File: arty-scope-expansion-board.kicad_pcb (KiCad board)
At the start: 4 copper layers, 109 x 86 mm, 131 parts, among them J1 PMOD_A, J2 PMOD_B, J3 PMOD_C, J4 PMOD_D, J5 Conn_Coaxial, J6 Conn_01x02_Pin, J7 Conn_Coaxial, U1 AD9288, U10 MCP1826S, U11 MIC5504-3.3YM5, U12 AD8132ARZ, U13 AD8370AREZ-RL7, U14 AD8132ARZ, U2 74LS374, U3 74LS374, U4 AD8370AREZ-RL7, U5 AD8132ARZ, U6 AD8132ARZ, U7 MCP4822, U8 74AHCT541, U9 74AHCT541

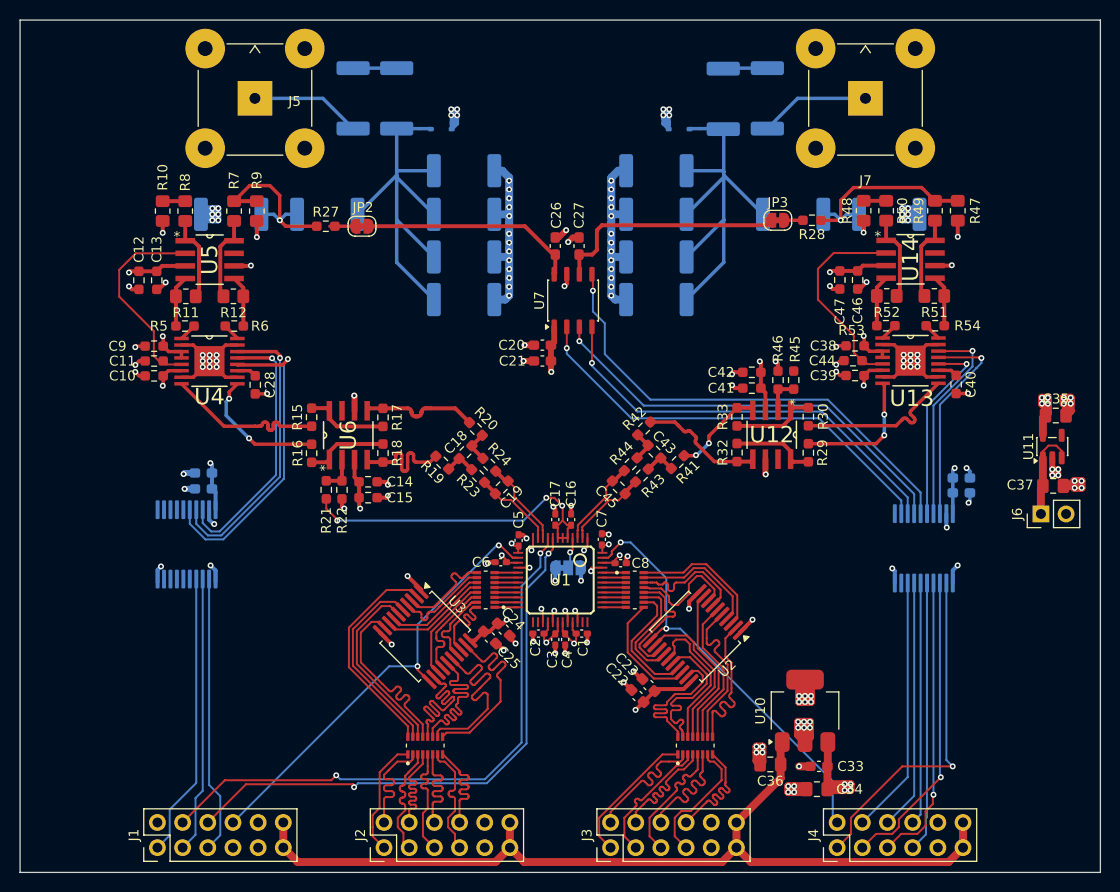
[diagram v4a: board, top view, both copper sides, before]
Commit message: [feat] Changed input stage routing, corrected DRC errors, added some silk labels
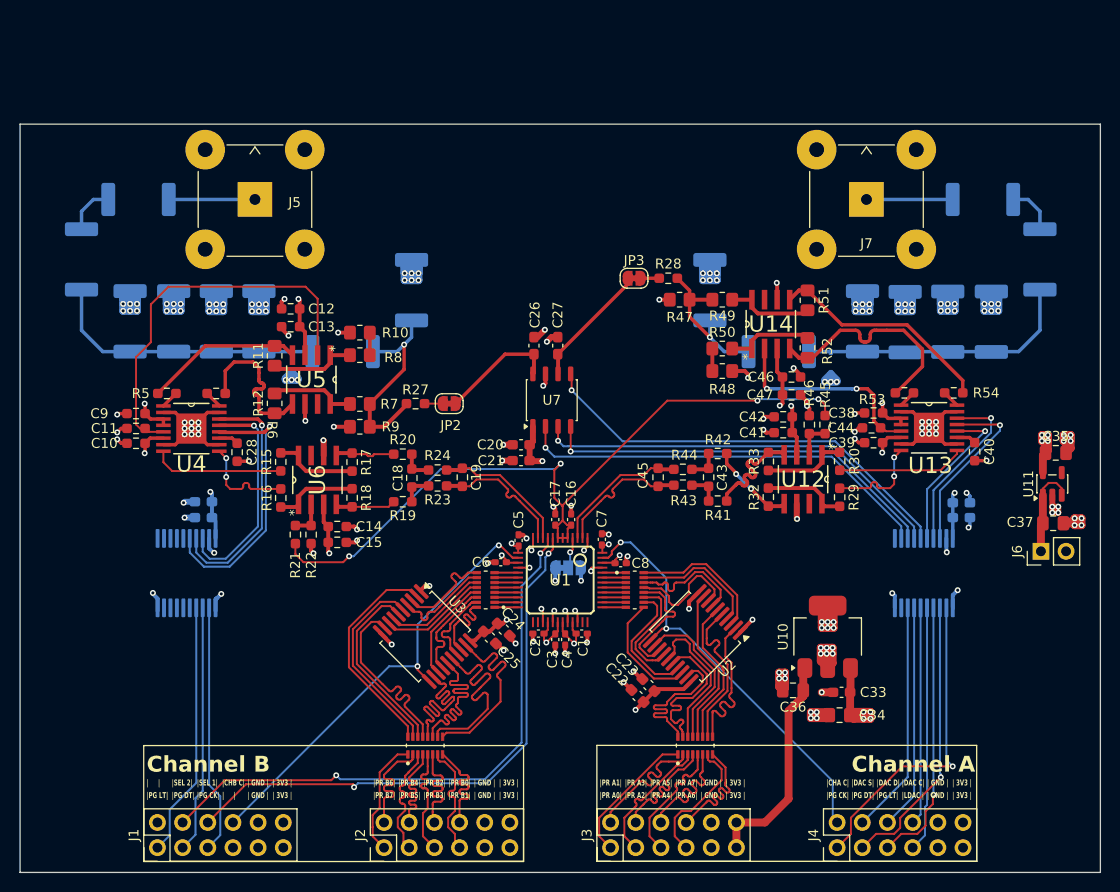
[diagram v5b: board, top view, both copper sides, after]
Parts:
- moved R35 37.1 mm to (213.5, 67.4), turned to 90 degrees
- moved R2 37.0 mm to (126.6, 67.4), turned to 90 degrees
- moved R34 35.8 mm to (218.4, 61.1)
- moved R13 35.7 mm to (121.7, 61.1)
- moved R36 31.3 mm to (209.1, 67.4), turned to 90 degrees
- moved R26 31.2 mm to (131.0, 67.4), turned to 90 degrees
- moved R47 29.5 mm to (182.1, 65.2), turned to 0 degrees
- moved D4 28.1 mm to (197.3, 71.5), turned to -90 degrees
- moved D3 27.9 mm to (142.9, 71.5), turned to -90 degrees
- moved R25 25.8 mm to (135.3, 67.4), turned to 90 degrees
- moved R38 25.2 mm to (204.8, 67.5), turned to 90 degrees
- moved R9 24.1 mm to (149.8, 78.0), turned to 0 degrees
- moved R31 24.0 mm to (212.7, 55.1), turned to 180 degrees
- moved R1 23.9 mm to (127.5, 55.1), turned to 0 degrees
- moved R10 23.4 mm to (149.8, 68.5), turned to 0 degrees
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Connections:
- J1 pad 11: VIN_3.3V -> unconnected-(J1-Pin_11-Pad11)
- J1 pad 12: VIN_3.3V -> unconnected-(J1-Pin_12-Pad12)
- J2 pad 11: VIN_3.3V -> unconnected-(J2-Pin_11-Pad11)
- J2 pad 12: VIN_3.3V -> unconnected-(J2-Pin_12-Pad12)
- J4 pad 11: VIN_3.3V -> unconnected-(J4-Pin_11-Pad11)
- J4 pad 12: VIN_3.3V -> unconnected-(J4-Pin_12-Pad12)
- R21 pad 1: REFOUT_VOCM -> REFOUT_VOCM_A
- R22 pad 2: REFOUT_VOCM -> REFOUT_VOCM_A
- R45 pad 1: REFOUT_VOCM -> REFOUT_VOCM_B
- R46 pad 2: REFOUT_VOCM -> REFOUT_VOCM_B
- U12 pad 2: REFOUT_VOCM -> REFOUT_VOCM_B
- U6 pad 2: REFOUT_VOCM -> REFOUT_VOCM_A
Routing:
- net VIN_3.3V: track 92.4 -> 22.7 mm
- net REFOUT: track 34.0 -> 76.8 mm, vias 3 -> 4
- net GND: track 233.7 -> 268.6 mm, vias 165 -> 184
- net VOCM_A: track 20.6 -> 40.0 mm
- net Net-(U14--OUT): track 5.18 -> 22.9 mm
- net Net-(U14-+OUT): track 5.18 -> 22.9 mm
- net Net-(D3-A1): track 42.3 -> 28.3 mm
- net Net-(D4-A1): track 42.3 -> 28.3 mm
- net Net-(JP3-A): track 24.2 -> 12.7 mm
- net Net-(U5-+OUT): track 5.18 -> 16.0 mm
- net Net-(U5--OUT): track 5.18 -> 15.9 mm
- net Net-(JP2-A): track 22.2 -> 12.3 mm
- net REFOUT_VOCM: track 7.44 -> 0.00 mm
- net Net-(U6-+OUT): track 11.9 -> 6.11 mm
- net Net-(U6--OUT): track 11.9 -> 6.16 mm
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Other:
- board size 109 x 86 mm -> 109 x 75.5 mm
- board text added: "Channel A"
- board text added: "Channel B"
- board text added: "R6"
- board text added: "| 3V3 |"
- board text added: "| GND |"
- board text added: "| |"
- board text added: "|CHA C|"
- board text added: "|CHB C|"
- board text added: "|DAC C|"
- board text added: "|DAC D|"
- board text added: "|DAC S|"
- board text added: "|LDAC |"
- board text added: "|PG CK|"
- board text added: "|PG DT|"
- board text added: "|PG LT|"
- board text added: "|PR A0|"
- board text added: "|PR A1|"
- board text added: "|PR A2|"
- board text added: "|PR A3|"
- board text added: "|PR A4|"
- board text added: "|PR A5|"
- board text added: "|PR A6|"
- board text added: "|PR A7|"
- board text added: "|PR B0|"
- board text added: "|PR B1|"
- board text added: "|PR B2|"
- board text added: "|PR B3|"
- board text added: "|PR B4|"
- board text added: "|PR B5|"
- board text added: "|PR B6|"
- board text added: "|PR B7|"
- board text added: "|SEL 1|"
- board text added: "|SEL 2|"

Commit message: [backup] ---
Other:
- board text added: "PMOD_A"
- board text added: "PMOD_B"
- board text added: "PMOD_C"
- board text added: "PMOD_D"
- board text added: "UWAGA TO ZŁĄCZE JEST NIE DO KUPIENIA"

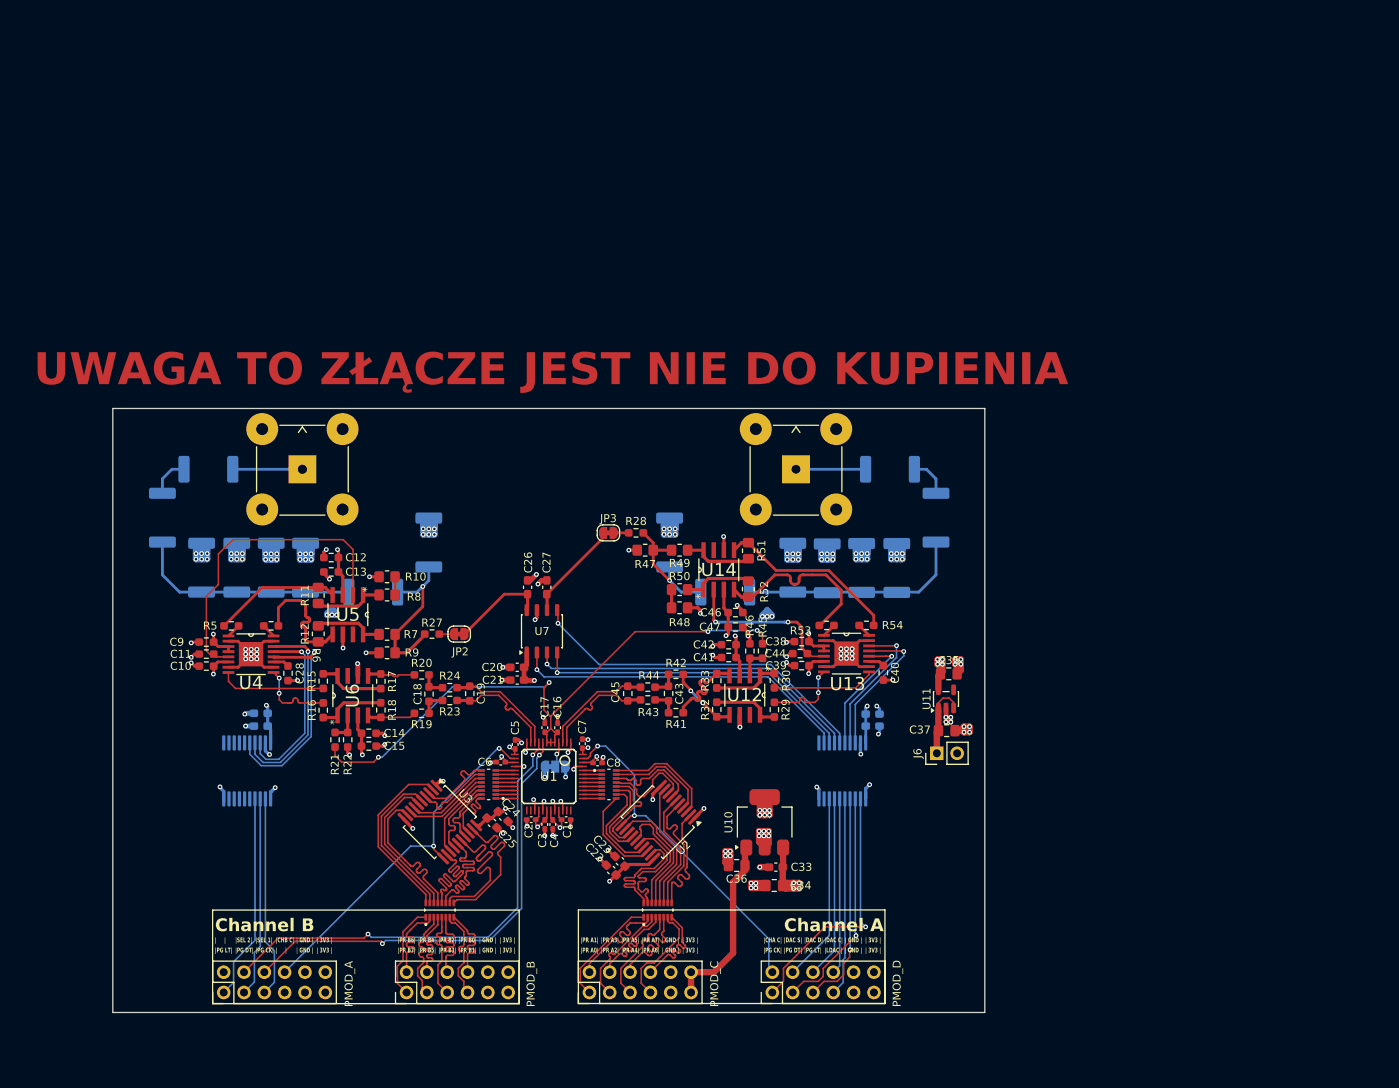
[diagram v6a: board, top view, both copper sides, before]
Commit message: [feat] Added stitching vias and filled top and bottom with ground
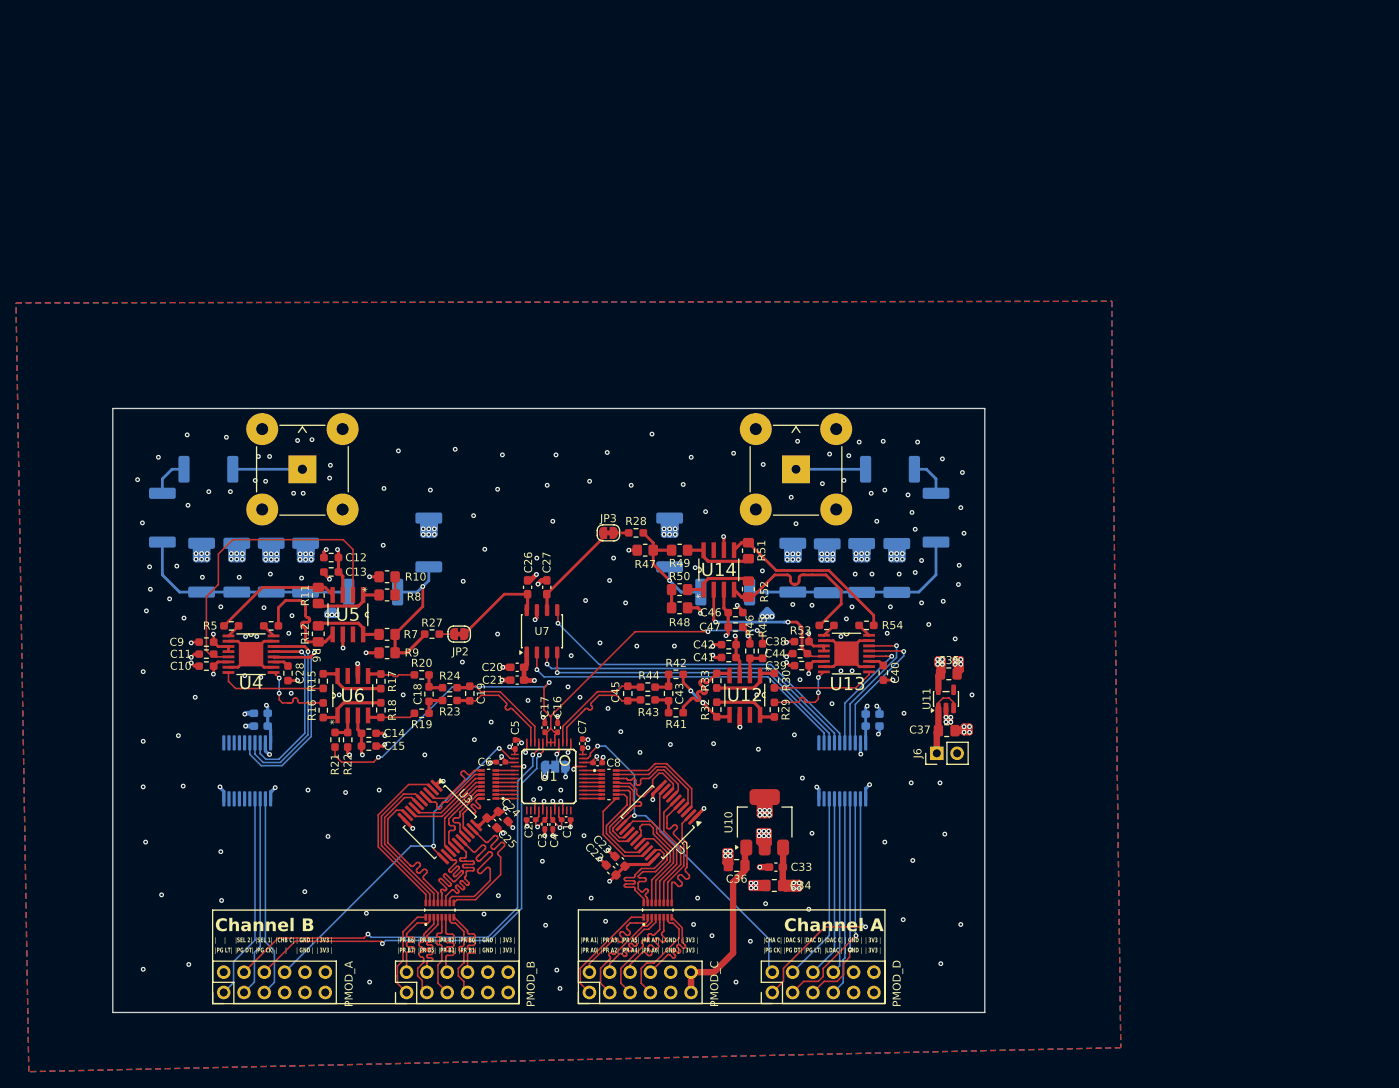
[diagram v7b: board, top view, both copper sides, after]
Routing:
- net GND: vias 184 -> 348
- added copper zone on B.Cu, net GND
- added copper zone on F.Cu, net GND
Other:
- board text removed: "UWAGA TO ZŁĄCZE JEST NIE DO KUPIENIA"

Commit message: [feat] Added test points and some labels on silkscreen
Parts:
- added ?: , , F.Cu at (202.0, 102.3)
- added ?: , , F.Cu at (216.5, 80.7)
- added ?: , , F.Cu at (177.0, 88.5)
- added ?: , , F.Cu at (191.7, 100.9)
- added REF**: TestPoint_Pad_D2.0mm, TestPoint:TestPoint_Pad_D2.0mm, F.Cu at (122.0, 98.3)
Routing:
- net VIN_3.3V: track 22.7 -> 26.9 mm
- net +3.3VCC: track 39.9 -> 42.6 mm
- net +5VCC: track 57.8 -> 60.2 mm
- net CH_A_CLK: track 43.5 -> 45.1 mm
- net GND: vias 348 -> 349
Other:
- board text added: "CLK A"
- board text added: "GND"
- board text added: "TEST GND"
- board text added: "VCC"
- board text added: "VIN"
- board text added: "VOUT"
